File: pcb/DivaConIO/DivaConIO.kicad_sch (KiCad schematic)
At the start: 32 parts, among them J1 DPad Buttons, J10 SWD, J2 Slider i2c, J3 Display i2c, J4 Face Buttons, J5 Button LEDs, J6 L Buttons, J7 Fn Buttons, J8 R Buttons, J9 Slider LEDs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

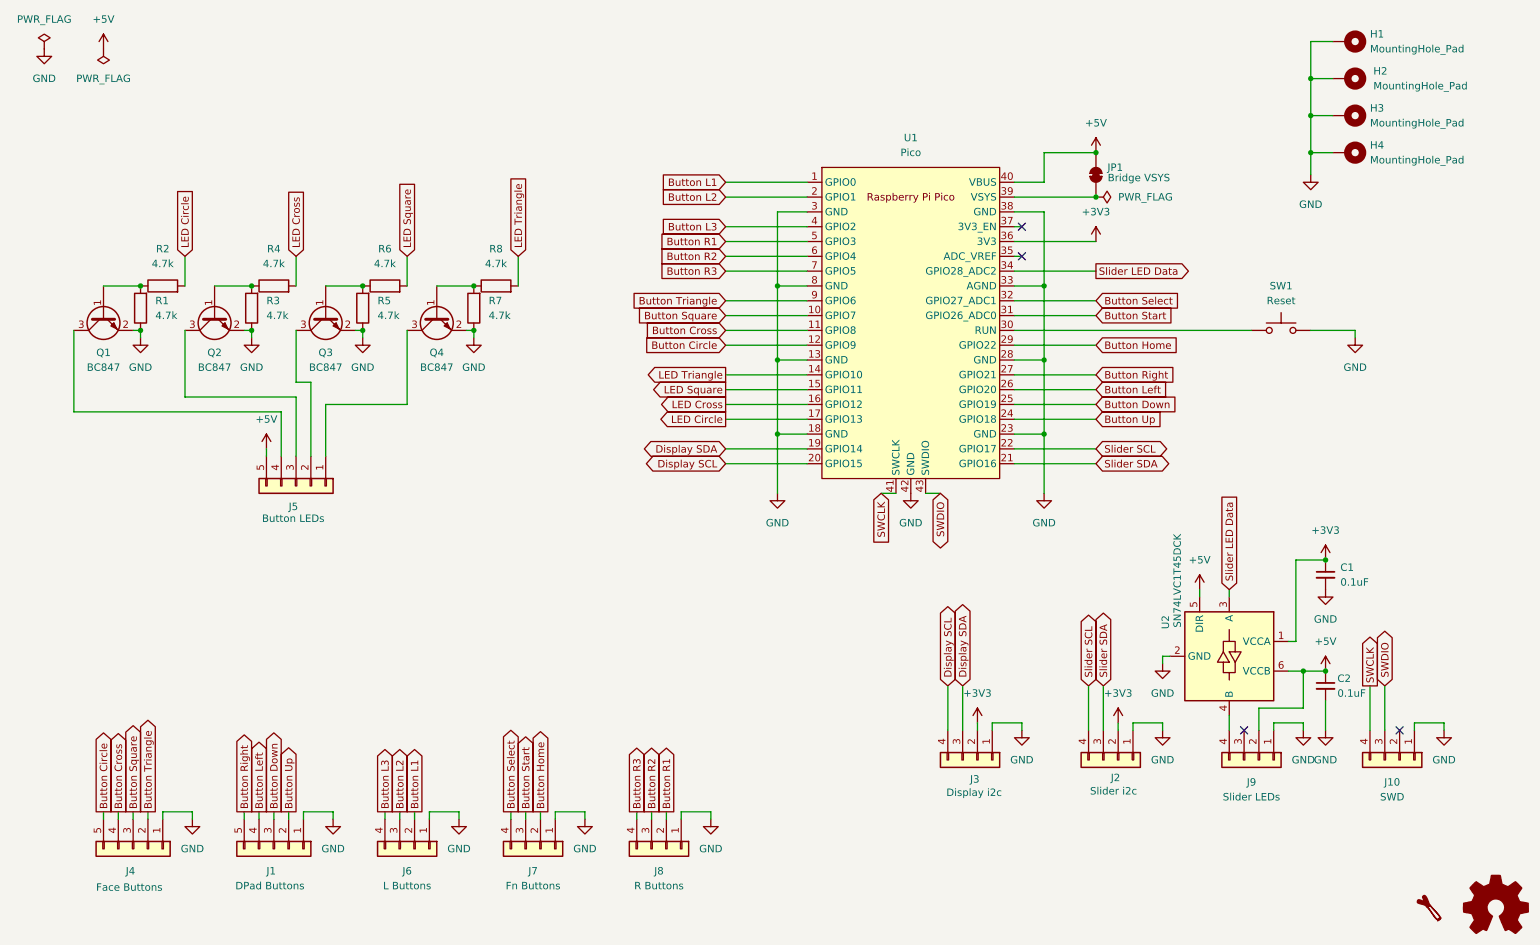
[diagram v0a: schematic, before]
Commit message: DivaConIO revision 2
- Changed JP1 to allow external power supply
- Added +5V to empty pin on SWD connector
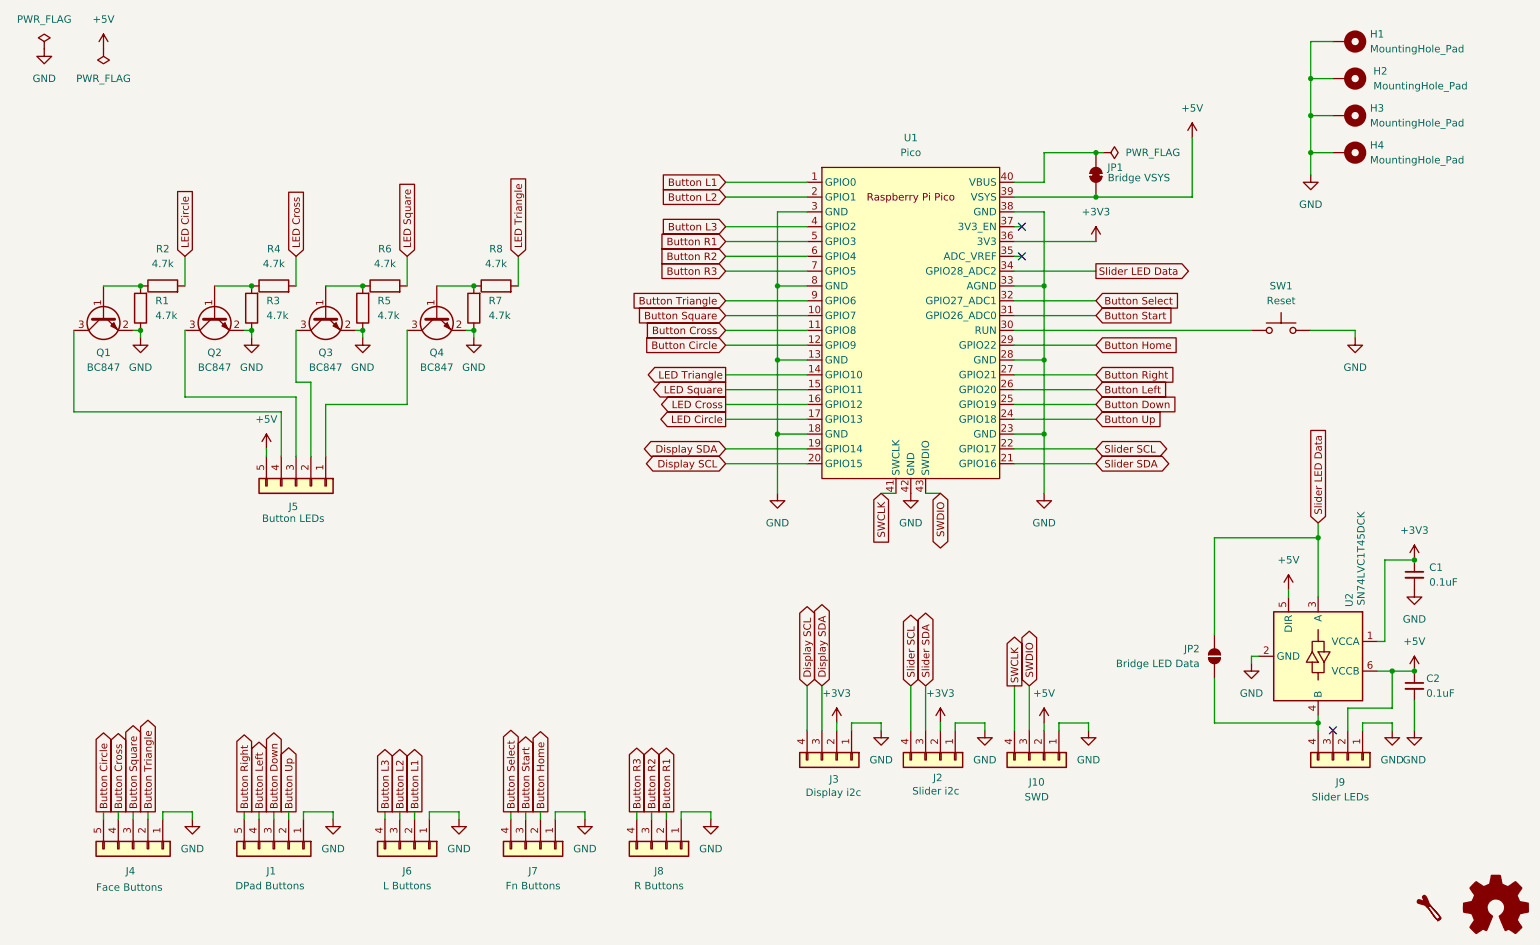
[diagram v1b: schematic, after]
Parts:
- added JP2: Bridge LED Data, Jumper:SolderJumper-2_P1.3mm_Open_RoundedPad1.0x1.5mm, symbol Jumper:SolderJumper_2_Open
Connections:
- net +5V: now also J10.2 (Pin_2), JP1.1 (A), U1.39 (VSYS); no longer JP1.2 (B), U1.40 (VBUS)
- net Slider LED Data: now also JP2.1 (A)
- net at J9.4 (Pin_4), U2.4 (B): now also JP2.2 (B)
- new net: JP1.2 (B), U1.40 (VBUS)
- no-connect marks 4 -> 3
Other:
- moved on the sheet: C1, C2, J10, J2, J3, J9, U2
